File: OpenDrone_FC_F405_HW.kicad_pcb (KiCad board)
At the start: 8 copper layers, 34 x 34 mm, 105 parts, among them J1 Conn_01x05, J10 Conn_01x02, J12 Conn_01x02, J13 Conn_01x02, J14 Conn_01x02, J15 Conn_01x02, J16 Conn_01x02, J17 Conn_01x02, J19 Conn_01x02, J2 Conn_01x02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

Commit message: update project
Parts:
- removed C30, C34, C42: 10uF, Capacitor_SMD:C_1210_3225Metric
- removed C31, C32, C35: 100nF, Capacitor_SMD:C_0402_1005Metric
- removed C33, C40, C41: 100nF, Capacitor_SMD:C_1210_3225Metric
- removed C36: 47uF, Capacitor_SMD:C_0402_1005Metric
- removed C37: 22uF, Capacitor_SMD:C_0402_1005Metric
- removed C38: 1nF, Capacitor_SMD:C_0402_1005Metric
- removed C43: 10uF, Capacitor_SMD:C_0805_2012Metric
- removed D5: SS34, Diode_SMD:D_SMA
- removed J15, J17, J19, J20, J21: Conn_01x02, Footprint:MountingPad_1x2
- removed R14, R15: 75R, Resistor_SMD:R_0402_1005Metric
- removed R18: 1k, Resistor_SMD:R_0402_1005Metric
- removed R4, R6: 10k, Resistor_SMD:R_0402_1005Metric
- removed U7: AT7456, Package_SO:TSSOP-28-1EP_4.4x9.7mm_P0.65mm
- removed U9: Ai-Thinker-Ra-02, Footprint:Ai-Thinker-Ra-02-LoRa
- removed Y2: 8MHz, Crystal:Crystal_SMD_3225-4Pin_3.2x2.5mm
- added J11: Conn_01x05, Connector_PinHeader_2.00mm:PinHeader_1x05_P2.00mm_Vertical, F.Cu at (161.8, 74.8)
- added J3: Conn_01x02, Footprint:HolePad_1x2, F.Cu at (136.3, 67.2)
- C19: value TBD -> 10nF
- J12, J16: value Conn_01x02 -> Conn_01x05; footprint Footprint:MountingPad_1x2 -> Connector_PinHeader_2.00mm:PinHeader_1x05_P2.00mm_Vertical; moved to F.Cu
- J13, J14, J2, J9: footprint Footprint:MountingPad_1x2 -> Footprint:HolePad_1x2; moved to F.Cu
- J4: value USB_A -> Conn_01x02; footprint Footprint:USB_Micro-B_SMD -> Footprint:HolePad_1x2
- J5: footprint Footprint:MountingPad_1x2 -> Footprint:HolePad_1x2
- J7: value Conn_01x04 -> Conn_01x02; footprint Footprint:MountingPad_1x4 -> Footprint:HolePad_1x2; moved to F.Cu
- moved J13 32.6 mm to (162.3, 99.5)
- moved J14 32.4 mm to (166.7, 95.2)
- moved J16 32.1 mm to (165.8, 74.8), turned to 0 degrees
- moved J12 28.6 mm to (163.8, 74.8), turned to 0 degrees
- moved J9 27.6 mm to (134.3, 97.4), turned to 90 degrees
- moved R7 26.2 mm to (140.5, 73.8), turned to -90 degrees
- moved R8 24.3 mm to (141.4, 73.8), turned to -90 degrees
- moved J5 22.5 mm to (134.3, 69.2), turned to -90 degrees
- moved J2 19.3 mm to (136.4, 99.5), turned to 0 degrees
- moved R2 18.6 mm to (146.2, 71.9), turned to -90 degrees
- moved J7 15.1 mm to (166.6, 71.4), turned to 90 degrees
- moved J4 13.1 mm to (162.4, 67.1), turned to 0 degrees
- moved C22 11.7 mm to (144.7, 83.5), turned to 0 degrees
- moved C23 8.17 mm to (140.4, 71.9), turned to 90 degrees
- moved R1 7.44 mm to (147.2, 71.9), turned to -90 degrees
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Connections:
- J12 pad 1: +5V -> SPI2_CS
- J12 pad 2: GND -> SPI2_CLK
- J13 pad 1: UART6_TX -> +5V
- J13 pad 2: UART6_RX -> GND
- J14 pad 1: STM32_PB10 -> +3V3
- J14 pad 2: STM32_PB11 -> GND
- J16 pad 1: RCIN_INT -> STM32_PB10
- J16 pad 2: RSSI_IN -> STM32_PB11
- J2 pad 1: OSD_VID_IN -> +5V
- J2 pad 2: OSD_VID_OUT -> GND
- J4 pad 1: 5V_USB -> +3V3
- J4 pad 2: USB_D- -> GND
- J7 pad 1: SPI1_CS -> UART6_TX
- J7 pad 2: SPI1_CLK -> UART6_RX
- J9 pad 1: ALARM -> LED_STRIP
- J9 pad 2: LED_STRIP -> ALARM
- U1 pad 14: SENS_RSSI -> unconnected-(U1-PA0-Pad14)
- U1 pad 25: SENS_USB -> unconnected-(U1-PC5-Pad25)
- U1 pad 44: USB_D- -> unconnected-(U1-PA11-Pad44)
- U1 pad 45: USB_D+ -> unconnected-(U1-PA12-Pad45)
- U1 pad 50: OSD_CS -> unconnected-(U1-PA15-Pad50)
- U1 pad 51: SPI3_CLK -> unconnected-(U1-PC10-Pad51)
- U1 pad 52: SPI3_MISO -> unconnected-(U1-PC11-Pad52)
- U1 pad 53: SPI3_MOSI -> unconnected-(U1-PC12-Pad53)
- U1 pad 55: BMP280_CS -> unconnected-(U1-PB3-Pad55)
- U1 pad 61: RCIN_INT -> unconnected-(U1-PB8-Pad61)
- U6 pad 2: BMP280_CS -> unconnected-(U6-CSB-Pad2)
- U6 pad 3: SPI3_MOSI -> I2C1_SDA
- U6 pad 4: SPI3_CLK -> I2C1_SCL
- U6 pad 5: SPI3_MISO -> unconnected-(U6-SDO-Pad5)
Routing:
- net +3V3: track 144.3 -> 0.00 mm, vias 36 -> 0
- net +5V: track 67.3 -> 0.00 mm, vias 22 -> 0
- net SPI3_CLK: track 44.2 -> 0.00 mm, vias 3 -> 0
- net 3V3_DEBUGGER: track 43.4 -> 0.00 mm
- net I2C1_SDA: track 42.8 -> 0.00 mm, vias 4 -> 0
- net STM32_PB10: track 41.7 -> 0.00 mm, vias 2 -> 0
- net I2C1_SCL: track 41.1 -> 0.00 mm, vias 4 -> 0
- net SPI3_MOSI: track 40.4 -> 0.00 mm, vias 3 -> 0
- net SPI3_MISO: track 37.7 -> 0.00 mm, vias 3 -> 0
- net STM32_PB11: track 35.9 -> 0.00 mm, vias 2 -> 0
- net V_BAT: track 35.9 -> 0.00 mm, vias 18 -> 0
- net LORA_RST: track 35.7 -> 0.00 mm, vias 2 -> 0
- net 5V_USB: track 34.9 -> 0.00 mm, vias 4 -> 0
- net LED_GREEN: track 30.6 -> 0.00 mm, vias 2 -> 0
- net LED_BLUE: track 29.7 -> 0.00 mm, vias 2 -> 0
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- removed copper zone on B.Cu, net +3V3
- removed copper zone on F.Cu, net +3V3
- removed copper zone on In1.Cu, net +3V3
- removed copper zone on B.Cu, net +5V
- removed copper zone on In1.Cu, net +5V
- removed copper zone on In6.Cu, net +5V
- removed copper zone on F.Cu, net 5V_USB
- removed copper zone on In1.Cu, net GND
- removed copper zone on In2.Cu, net GND
- removed copper zone on In3.Cu, net GND
- removed copper zone on In4.Cu, net GND
- removed copper zone on In5.Cu, net GND
- removed copper zone on In6.Cu, net GND
- removed copper zone on In1.Cu, net V_BAT
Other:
- copper layers 8 -> 2

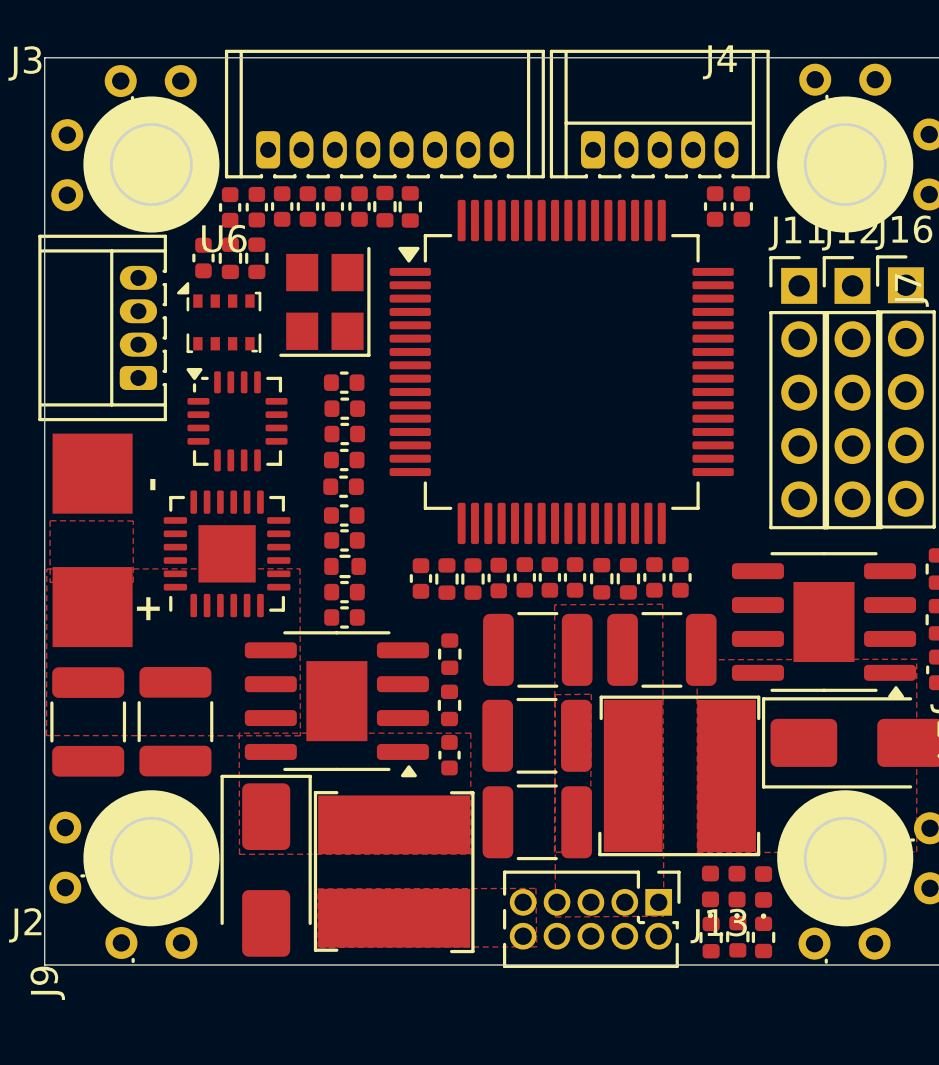
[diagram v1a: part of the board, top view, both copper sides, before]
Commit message: update placement
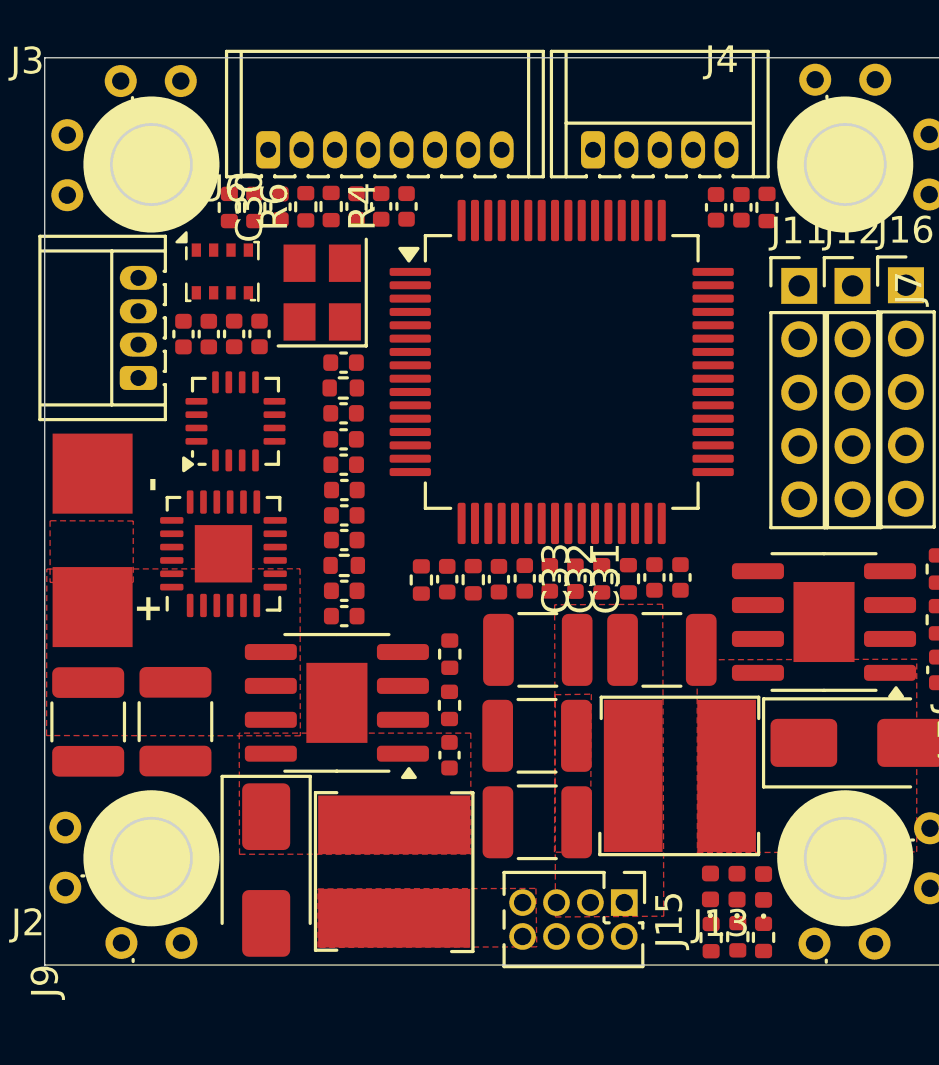
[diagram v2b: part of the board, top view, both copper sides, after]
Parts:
- removed C44, C45, C46: 100nF, Capacitor_SMD:C_0402_1005Metric
- removed J22: Conn_02x05_Odd_Even, Connector_PinHeader_1.27mm:PinHeader_2x05_P1.27mm_Vertical
- added C30: 100nF, Capacitor_SMD:C_0402_1005Metric, F.Cu at (142.3, 71.9)
- added C31: 100nF, Capacitor_SMD:C_0402_1005Metric, F.Cu at (153.4, 85.8)
- added C32: 100nF, Capacitor_SMD:C_0402_1005Metric, F.Cu at (152.4, 85.8)
- added C33: 100nF, Capacitor_SMD:C_0402_1005Metric, F.Cu at (151.5, 85.8)
- added J15: Conn_02x04_Odd_Even, Connector_PinHeader_1.27mm:PinHeader_2x04_P1.27mm_Vertical, F.Cu at (155.2, 98.0)
- added R4: Rf_Cur, Resistor_SMD:R_0402_1005Metric, F.Cu at (144.2, 71.9)
- added R6: Ri_Cur, Resistor_SMD:R_0402_1005Metric, F.Cu at (143.3, 71.9)
- moved R2 14.3 mm to (160.6, 71.9)
- moved C23 11.4 mm to (144.7, 82.5), turned to 0 degrees
- moved C24 9.36 mm to (144.7, 81.5), turned to 0 degrees
- moved R1 7.23 mm to (144.7, 78.7), turned to 0 degrees
- moved C29 6.68 mm to (138.7, 76.7), turned to -90 degrees
- moved C28 5.08 mm to (139.7, 76.7), turned to -90 degrees
- moved C25 5.00 mm to (140.6, 76.7), turned to -90 degrees
- moved C26 4.93 mm to (141.6, 76.7), turned to 90 degrees
- moved C21 3.00 mm to (144.7, 84.4)
- moved C22 2.85 mm to (144.7, 80.6)
- moved C9 2.78 mm to (145.2, 71.9)
- moved C5 2.75 mm to (144.7, 79.6), turned to 0 degrees
- moved R10 1.94 mm to (147.6, 85.9)
- moved U6 1.91 mm to (140.2, 74.3)
- moved R8 1.91 mm to (141.4, 71.9)
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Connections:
- J6 pad 4: SENS_CUR -> IN_CUR
- U1 pad 15: unconnected-(U1-PA1-Pad15) -> MPU6000_INT
- U1 pad 24: MPU6000_INT -> unconnected-(U1-PC4-Pad24)

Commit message: update project
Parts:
- removed J15: Conn_02x04_Odd_Even, Connector_PinHeader_1.27mm:PinHeader_2x04_P1.27mm_Vertical
- added J17: Conn_02x03_Odd_Even, Connector_PinHeader_1.27mm:PinHeader_2x03_P1.27mm_Vertical, F.Cu at (154.0, 98.0)
- moved D3 2.61 mm to (157.8, 97.3), turned to 180 degrees
- moved R17 2.08 mm to (159.7, 97.3), turned to 0 degrees
- moved D2 2.05 mm to (157.8, 99.3), turned to 180 degrees
- moved D6 1.89 mm to (157.8, 98.3), turned to 180 degrees
- moved R16 1.25 mm to (159.7, 99.3), turned to 0 degrees
- moved R25 0.98 mm to (159.7, 98.3), turned to 0 degrees
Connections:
- J11 pad 1: SPI1_CS -> LORA_IRQ
- J11 pad 2: SPI1_CLK -> SPI2_MOSI
- J11 pad 3: SPI1_MISO -> SPI2_MISO
- J11 pad 4: SPI1_MOSI -> SPI2_CLK
- J11 pad 5: LORA_RST -> SPI2_CS
- J12 pad 1: SPI2_CS -> LORA_RST
- J12 pad 2: SPI2_CLK -> unconnected-(J12-Pin_2-Pad2)
- J12 pad 3: SPI2_MISO -> unconnected-(J12-Pin_3-Pad3)
- J12 pad 4: SPI2_MOSI -> unconnected-(J12-Pin_4-Pad4)
- J12 pad 5: LORA_IRQ -> unconnected-(J12-Pin_5-Pad5)
- U1 pad 28: LORA_IRQ -> unconnected-(U1-PB2-Pad28)
- U1 pad 44: unconnected-(U1-PA11-Pad44) -> LORA_RST
- U1 pad 45: unconnected-(U1-PA12-Pad45) -> LORA_IRQ
- U1 pad 57: LORA_RST -> unconnected-(U1-PB5-Pad57)
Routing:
- net +3V3: track 0.00 -> 53.0 mm
- net Net-(U2-PH): track 0.00 -> 11.3 mm, vias 0 -> 2
- net MPU6000_XDA: track 0.00 -> 9.13 mm, vias 0 -> 2
- net V_BAT: track 0.00 -> 8.49 mm, vias 0 -> 2
- net MPU6000_XCL: track 0.00 -> 7.42 mm, vias 0 -> 2
- net Net-(U1-PH0): track 0.00 -> 6.11 mm
- net LORA_RST: track 0.00 -> 5.84 mm
- net SPI2_MOSI: track 0.00 -> 5.28 mm
- net +5V: track 0.00 -> 4.62 mm
- net Net-(U1-PH1): track 0.00 -> 4.41 mm
- net SPI2_MISO: track 0.00 -> 4.04 mm
- net SPI2_CS: track 0.00 -> 3.65 mm
- net LORA_IRQ: track 0.00 -> 3.63 mm
- net SPI2_CLK: track 0.00 -> 3.42 mm
- net Net-(U4-REGOUT): track 0.00 -> 3.05 mm
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
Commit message: update project
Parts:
- removed J10: Conn_01x02, Footprint:MountingPad_Battery
- removed R19, R20: 4.7k, Resistor_SMD:R_0402_1005Metric
- added C34: 100nF, Capacitor_SMD:C_0402_1005Metric, F.Cu at (144.9, 78.6)
- added SW1: RESET, Footprint:Button_SMD_4.2x3.3x2.5mm, F.Cu at (149.3, 68.4)
- C15: footprint Capacitor_SMD:C_1210_3225Metric -> Capacitor_SMD:C_1206_3216Metric
- J11, J12, J16: footprint Connector_PinHeader_2.00mm:PinHeader_1x05_P2.00mm_Vertical -> Footprint:Header_1x05_P2.00mm_Vertical
- J17: footprint Connector_PinHeader_1.27mm:PinHeader_2x03_P1.27mm_Vertical -> Connector_PinHeader_2.00mm:PinHeader_2x03_P2.00mm_Vertical
- L1, L2: footprint Footprint:Inductor_SMD_5D28 -> Footprint:Inductor_SMD_4D28
- U6: footprint Package_LGA:Bosch_LGA-8_2x2.5mm_P0.65mm_ClockwisePinNumbering -> Footprint:LGA-8_2x2.5mm_P0.65mm
- moved J9 30.2 mm to (136.4, 67.3), turned to 0 degrees
- moved J5 26.1 mm to (134.5, 95.3)
- moved J6 22.4 mm to (137.0, 91.6), turned to 90 degrees
- moved R7 20.5 mm to (155.4, 85.9), turned to 90 degrees
- moved R8 19.1 mm to (154.5, 85.9), turned to 90 degrees
- moved R2 16.9 mm to (143.7, 71.8)
- moved U5 11.5 mm to (142.5, 68.6), turned to 0 degrees
- moved C23 10.9 mm to (142.8, 71.8), turned to 90 degrees
- moved C25 10.5 mm to (145.5, 67.4), turned to 90 degrees
- moved C24 10.2 mm to (141.8, 71.8), turned to 90 degrees
- moved C30 9.87 mm to (144.9, 81.4), turned to 180 degrees
- moved C22 9.58 mm to (140.9, 71.8), turned to 90 degrees
- moved R6 8.74 mm to (144.9, 80.5), turned to 180 degrees
- moved C26 8.39 mm to (145.5, 69.3), turned to -90 degrees
- moved C21 8.14 mm to (139.0, 78.6), turned to -90 degrees
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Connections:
- J1 pad 2: STM32_DIO -> GND
- J1 pad 3: STM32_CLK -> STM32_NRST
- J1 pad 4: STM32_NRST -> STM32_CLK
- J1 pad 5: GND -> STM32_DIO
- J11 pad 1: LORA_IRQ -> SPI2_MOSI
- J11 pad 2: SPI2_MOSI -> SPI2_MISO
- J11 pad 3: SPI2_MISO -> SPI2_CLK
- J11 pad 4: SPI2_CLK -> SPI2_CS
- J11 pad 5: SPI2_CS -> +3V3
- J12 pad 2: unconnected-(J12-Pin_2-Pad2) -> LORA_IRQ
- J12 pad 3: unconnected-(J12-Pin_3-Pad3) -> I2C1_SDA
- J12 pad 4: unconnected-(J12-Pin_4-Pad4) -> I2C1_SCL
- J12 pad 5: unconnected-(J12-Pin_5-Pad5) -> GND
- J14 pad 1: +3V3 -> UART4_TX
- J14 pad 2: GND -> UART4_RX
- J16 pad 1: STM32_PB10 -> SPI1_CS
- J16 pad 2: STM32_PB11 -> SPI1_CLK
- J16 pad 3: +5V -> SPI1_MISO
- J16 pad 4: GND -> SPI1_MOSI
- J16 pad 5: +3V3 -> +5V
- J17 pad 1: 3V3_STEPDOWN -> 3V3_DEBUGGER
- J17 pad 3: 3V3_DEBUGGER -> 3V3_STEPDOWN
- J3 pad 1: +3V3 -> +5V
- J4 pad 1: +3V3 -> +5V
- J5 pad 1: I2C1_SCL -> I2C2_SCL
- J5 pad 2: I2C1_SDA -> I2C2_SDA
- J9 pad 1: LED_STRIP -> LED_STRIP1
- J9 pad 2: ALARM -> LED_STRIP2
- R7 pad 2: I2C1_SDA -> I2C2_SDA
- R8 pad 2: I2C1_SCL -> I2C2_SCL
- U1 pad 11: unconnected-(U1-PC3-Pad11) -> MPU6000_INT
- U1 pad 14: unconnected-(U1-PA0-Pad14) -> UART4_TX
- U1 pad 15: MPU6000_INT -> UART4_RX
- U1 pad 16: ESC4 -> ESC1
- U1 pad 17: ESC3 -> ESC2
- U1 pad 2: LED_GREEN -> unconnected-(U1-PC13-Pad2)
- U1 pad 26: ESC1 -> ESC3
- U1 pad 27: ESC2 -> ESC4
- U1 pad 29: STM32_PB10 -> I2C2_SCL
- U1 pad 3: LED_BLUE -> unconnected-(U1-PC14-Pad3)
- U1 pad 30: STM32_PB11 -> I2C2_SDA
- U1 pad 39: unconnected-(U1-PC8-Pad39) -> LED_GREEN
- U1 pad 4: LED_STRIP -> unconnected-(U1-PC15-Pad4)
- U1 pad 40: unconnected-(U1-PC9-Pad40) -> LED_BLUE
- U1 pad 61: unconnected-(U1-PB8-Pad61) -> LED_STRIP2
- U1 pad 62: unconnected-(U1-PB9-Pad62) -> LED_STRIP1
- U1 pad 8: ALARM -> unconnected-(U1-PC0-Pad8)
- U4 pad 23: I2C1_SCL -> I2C2_SCL
- U4 pad 24: I2C1_SDA -> I2C2_SDA
- U6 pad 3: I2C1_SDA -> I2C2_SDA
- U6 pad 4: I2C1_SCL -> I2C2_SCL
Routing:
- net +5V: track 4.62 -> 102.1 mm, vias 0 -> 7
- net +3V3: track 53.0 -> 135.5 mm, vias 0 -> 20
- net I2C2_SDA: track 0.00 -> 66.1 mm, vias 0 -> 3
- net I2C2_SCL: track 0.00 -> 64.0 mm, vias 0 -> 3
- net 3V3_DEBUGGER: track 0.00 -> 51.8 mm, vias 0 -> 2
- net UART4_TX: track 0.00 -> 47.4 mm, vias 0 -> 1
- net UART4_RX: track 0.00 -> 44.9 mm, vias 0 -> 1
- net LED_BLUE: track 0.00 -> 33.9 mm, vias 0 -> 2
- net LED_GREEN: track 0.00 -> 30.1 mm, vias 0 -> 2
- net SPI1_CLK: track 0.00 -> 26.9 mm, vias 0 -> 1
- net SPI1_CS: track 0.00 -> 25.7 mm, vias 0 -> 1
- net ESC4: track 0.00 -> 23.7 mm, vias 0 -> 1
- net STM32_NRST: track 0.00 -> 23.4 mm
- net UART1_RX: track 0.00 -> 22.6 mm, vias 0 -> 1
- net UART1_TX: track 0.00 -> 22.6 mm, vias 0 -> 1
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- added copper zone on F.Cu, net +3V3
- removed copper zone on F.Cu, net +5V
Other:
- board text added: "CLK2"
- board text added: "CS2"
- board text added: "MI2"
- board text added: "MO2"
- board text added: "PA11"
- board text added: "PA12"
- board text removed: "G"
- board text removed: "RF"
- board text removed: "SCL2"
- board text removed: "SDA2"
- board text removed: "USB"

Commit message: update project
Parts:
- moved J2 5.80 mm to (134.5, 95.2), turned to -90 degrees
- moved C13 5.48 mm to (143.4, 93.4)
- moved J5 4.43 mm to (136.4, 99.3), turned to 0 degrees
- moved R3 2.15 mm to (143.4, 89.9)
- moved R5 2.04 mm to (143.4, 88.0)
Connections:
- J12 pad 3: I2C1_SDA -> I2C1_SCL
- J12 pad 4: I2C1_SCL -> I2C1_SDA
- J9 pad 1: LED_STRIP1 -> LED_STRIP2
- J9 pad 2: LED_STRIP2 -> LED_STRIP1
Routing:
- net 5V_STEPDOWN: track 6.63 -> 14.0 mm
- net Net-(D1-K): track 6.88 -> 0.00 mm, vias 2 -> 0
- net Net-(U2-VSENSE): track 7.06 -> 11.8 mm
- net Net-(U2-PH): track 1.64 -> 5.62 mm, vias 0 -> 2
- net LED_STRIP2: track 21.2 -> 24.3 mm
- net +3V3: track 135.5 -> 138.0 mm
- net I2C2_SCL: track 64.0 -> 66.4 mm, vias 3 -> 4
- net I2C1_SCL: track 17.9 -> 15.8 mm
- net +5V: track 102.1 -> 103.3 mm
- net ESC4: track 23.7 -> 22.6 mm
- net ESC2: track 15.3 -> 14.2 mm
- net ESC1: track 17.5 -> 16.4 mm
- net LED_BLUE: track 33.9 -> 32.9 mm
- net Net-(U3-PH): track 8.11 -> 7.33 mm
- net SPI1_CS: track 25.7 -> 25.1 mm
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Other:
- board text added: "CL2"
- board text added: "DA2"
- board text added: "FC_F405_HW"
- board text added: "G"
- board text added: "Github: phonght32"
- board text added: "OpenDrone"
- board text added: "R4"
- board text added: "T4"
- board text added: "V1.0"
- board text added: "WS1"
- board text added: "WS2"
- board text removed: "A"
- board text removed: "RCIN"
- board text removed: "RSSI"
- board text removed: "VIDI"
- board text removed: "VIDO"
- board text removed: "WS"

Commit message: update project
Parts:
- removed Y1: 8MHz, Crystal:Crystal_SMD_3225-4Pin_3.2x2.5mm
- added Y2: 8Mhz, Crystal:Crystal_SMD_3225-4Pin_3.2x2.5mm, F.Cu at (144.2, 75.0)
- D2: value LED_RED -> RED
- moved C13 1.20 mm to (143.4, 92.2)
- moved R3 0.12 mm to (143.4, 90.0)
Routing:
- net Net-(U1-PH0): track 5.61 -> 8.27 mm
- net Net-(D1-K): track 0.00 -> 1.97 mm
- net Net-(U2-PH): track 5.62 -> 4.14 mm
- net Net-(U2-VSENSE): track 11.8 -> 10.9 mm
- net 5V_STEPDOWN: track 14.0 -> 13.4 mm
- net GND: vias 89 -> 96
